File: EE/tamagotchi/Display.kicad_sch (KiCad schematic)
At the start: 36 parts, among them J3 Conn_01x07, Q1 Q_NMOS_GSD, Q2 Q_NMOS_GSD, Q3 Q_NMOS_GSD, Q7 Q_NMOS_GSD

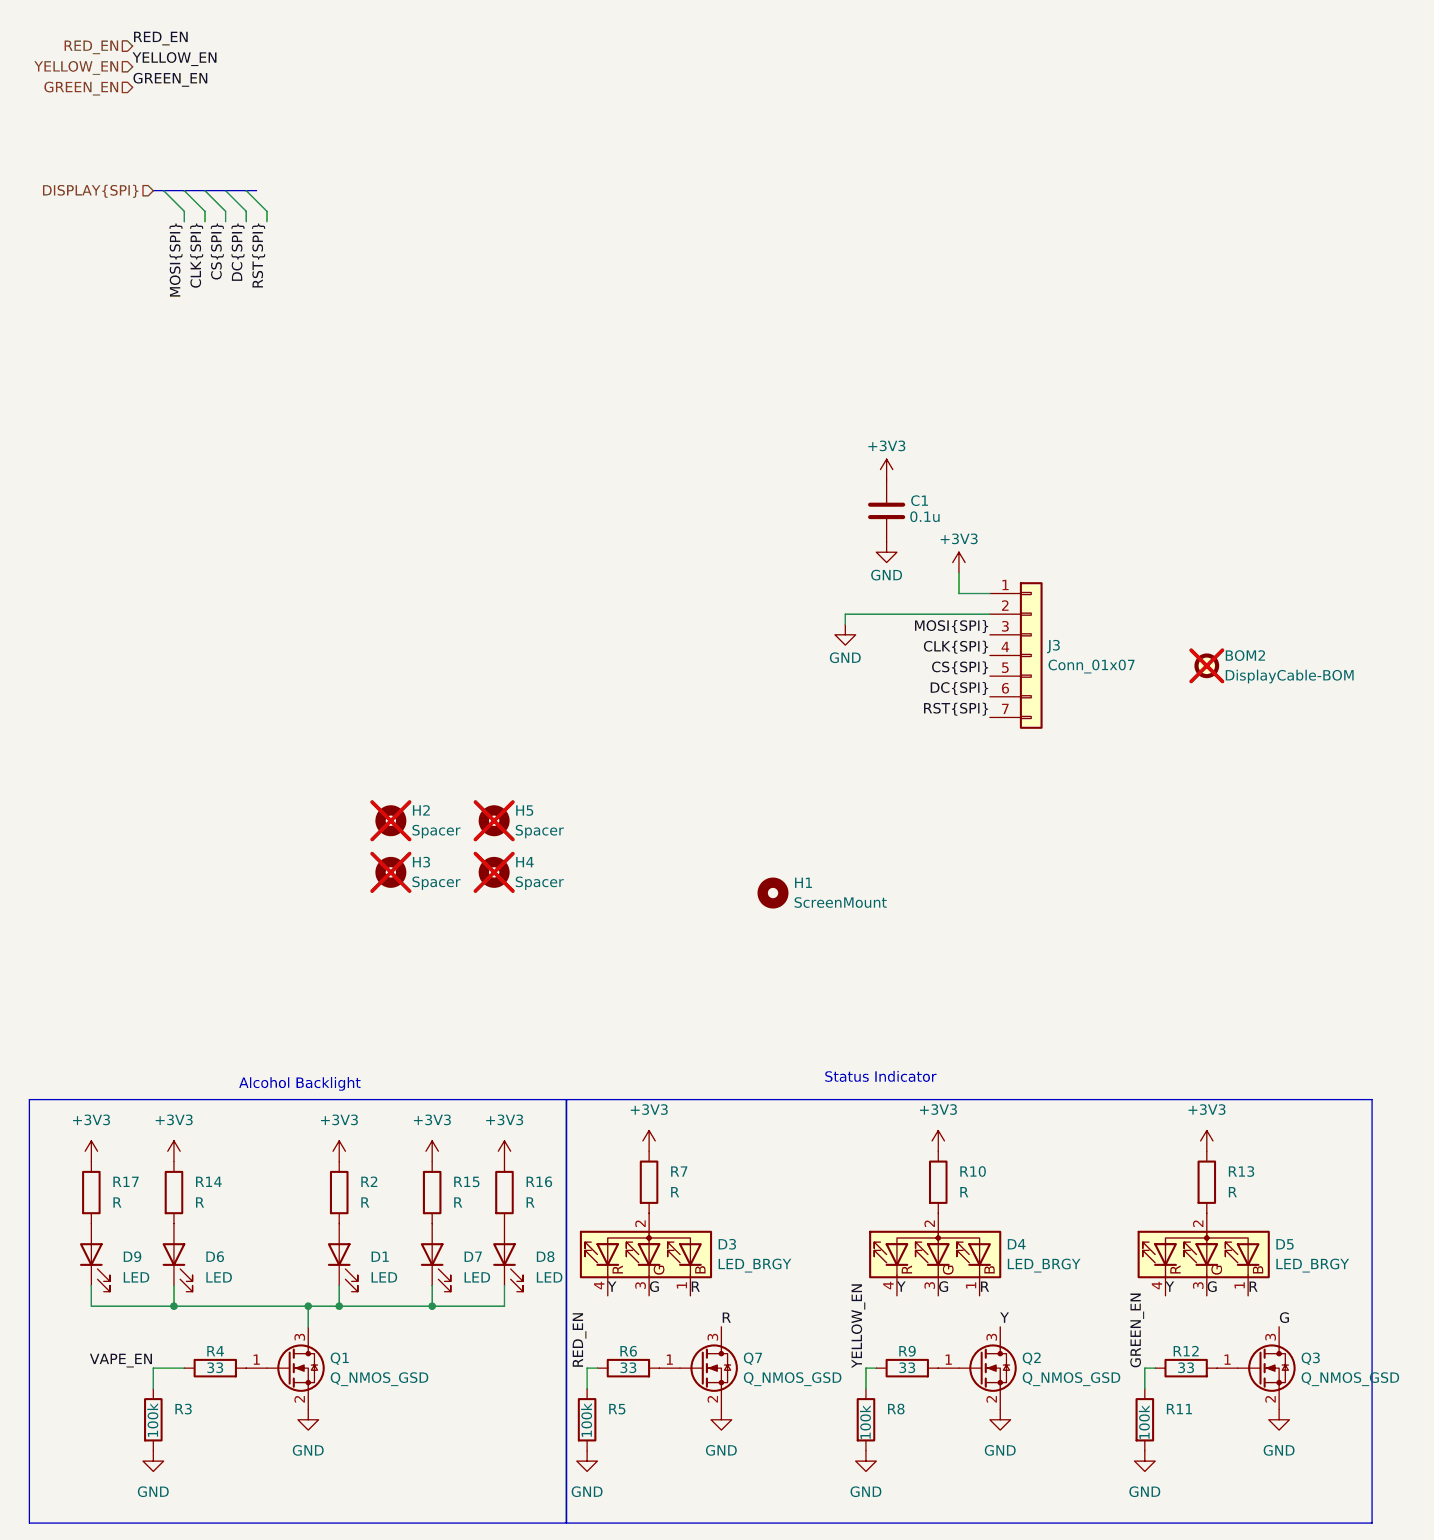
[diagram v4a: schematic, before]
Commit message: Removed LEDs
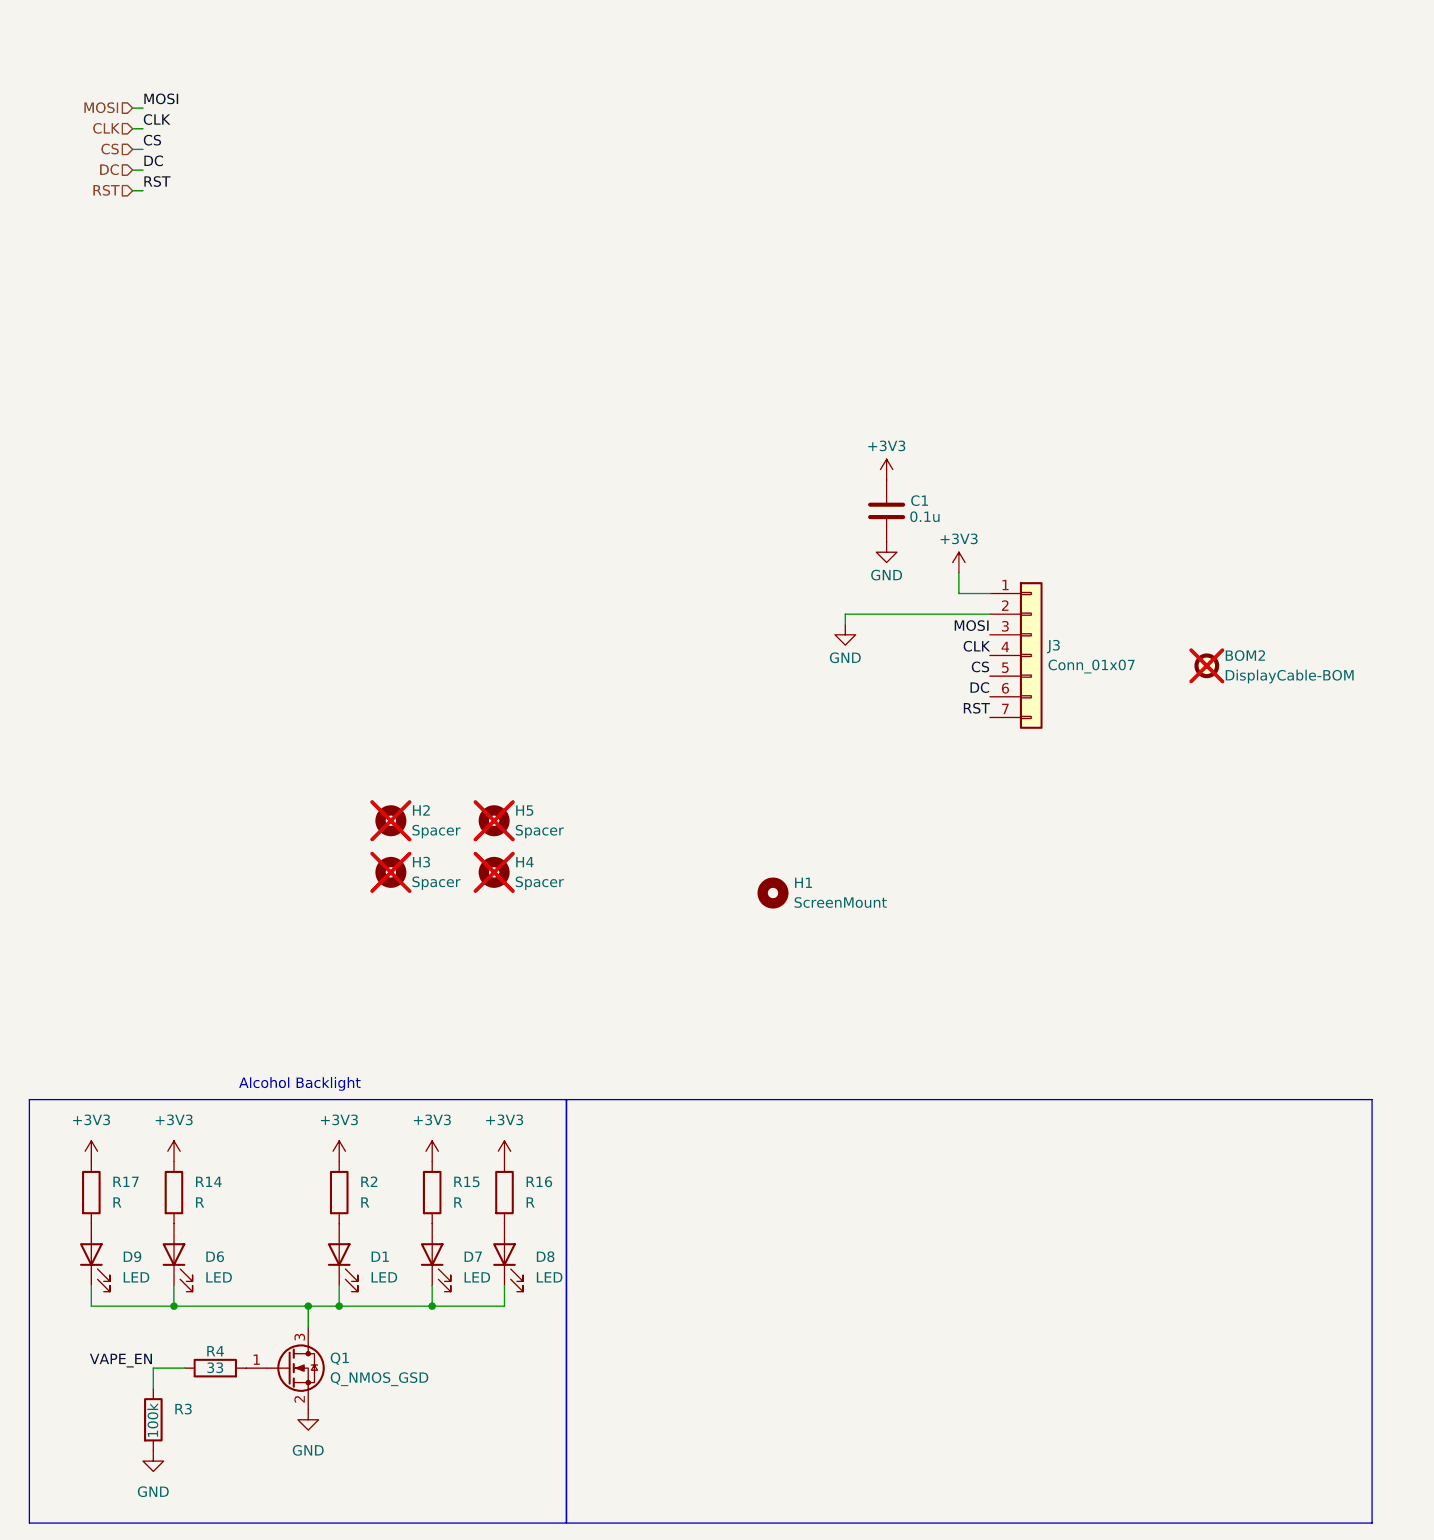
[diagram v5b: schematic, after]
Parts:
- removed D3, D4, D5: LED_BRGY, Library:EAST1616RGYA0_EVE, symbol Device:LED_BAGR
- removed Q2, Q3, Q7: Q_NMOS_GSD, Package_TO_SOT_SMD:SOT-23, symbol Transistor_FET:Q_NMOS_GSD
- removed R10, R13, R7: R, Resistor_SMD:R_0402_1005Metric_Pad0.72x0.64mm_HandSolder, symbol Device:R
- removed R11, R5, R8: 100k, Resistor_SMD:R_0402_1005Metric_Pad0.72x0.64mm_HandSolder, symbol Device:R
- removed R12, R6, R9: 33, Resistor_SMD:R_0402_1005Metric_Pad0.72x0.64mm_HandSolder, symbol Device:R
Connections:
- net CLK{SPI} renamed CLK
- net CS{SPI} renamed CS
- net DC{SPI} renamed DC
- net MOSI{SPI} renamed MOSI
- net RST{SPI} renamed RST
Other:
- note removed: "Status Indicator"

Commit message: First pass routing / placement & LED -> Buzzer for warning
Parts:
- added D2: D, Diode_SMD:D_0402_1005Metric_Pad0.77x0.64mm_HandSolder, symbol Device:D
- added LS1: SMT-0540-T-10-R, Library:XDCR_SMT-0540-T-10-R, symbol New_Library:SMT-0540-T-10-R
- added Q2: Q_NMOS_GSD, Package_TO_SOT_SMD:SOT-23, symbol Transistor_FET:Q_NMOS_GSD
- added R1: 100k, Resistor_SMD:R_0402_1005Metric_Pad0.72x0.64mm_HandSolder, symbol Device:R
- added R5: 33, Resistor_SMD:R_0402_1005Metric_Pad0.72x0.64mm_HandSolder, symbol Device:R
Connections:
- net +3V3: now also D2.1 (K), LS1.P
- net GND: now also Q2.2 (S), R1.2
- new net: D2.2 (A), LS1.N, Q2.3 (D)
- new net: Q2.1 (G), R5.2
- new net BUZZ_PWM: R1.1, R5.1
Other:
- note added: "Buzzer"
